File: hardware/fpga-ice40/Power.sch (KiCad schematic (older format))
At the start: 9 parts, among them J2 Conn_01x03, U8 AZ1117-1.2, U9 AZ1117-1.2

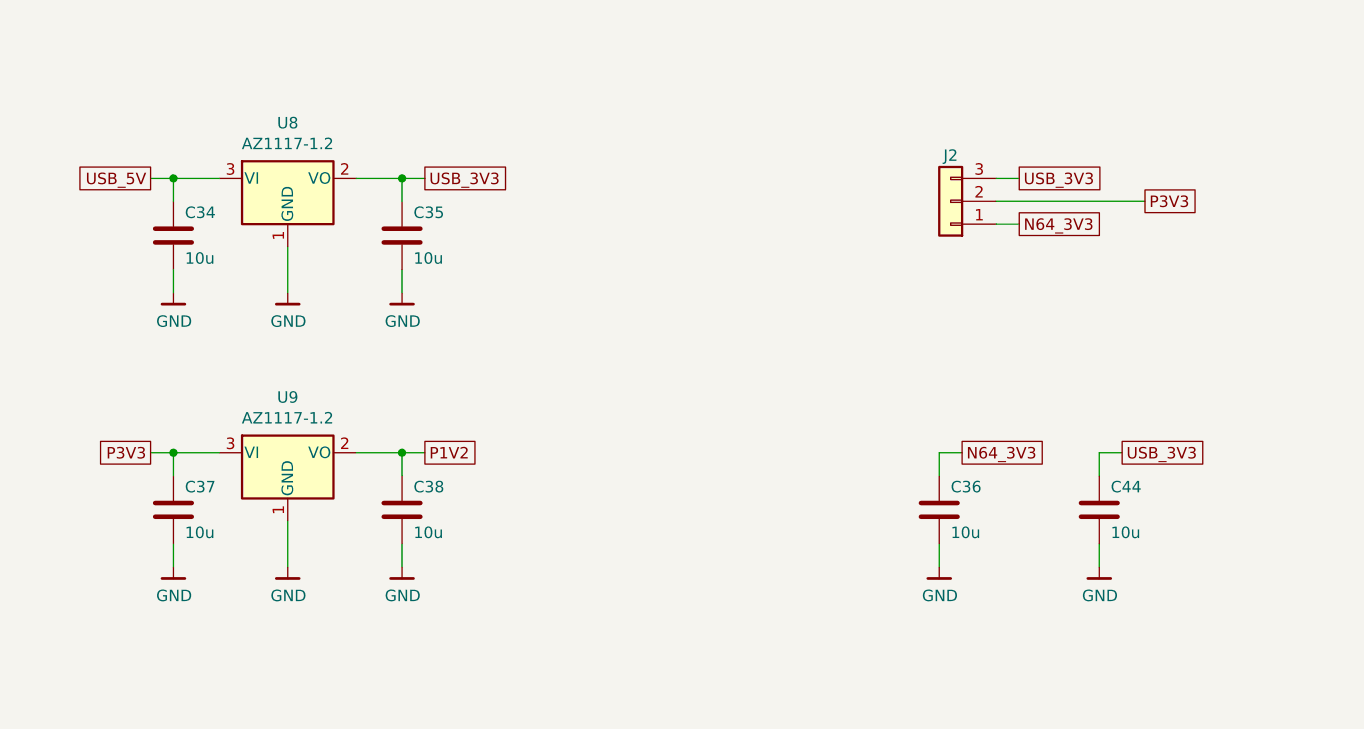
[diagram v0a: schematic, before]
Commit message: Add title and licensing info to documents
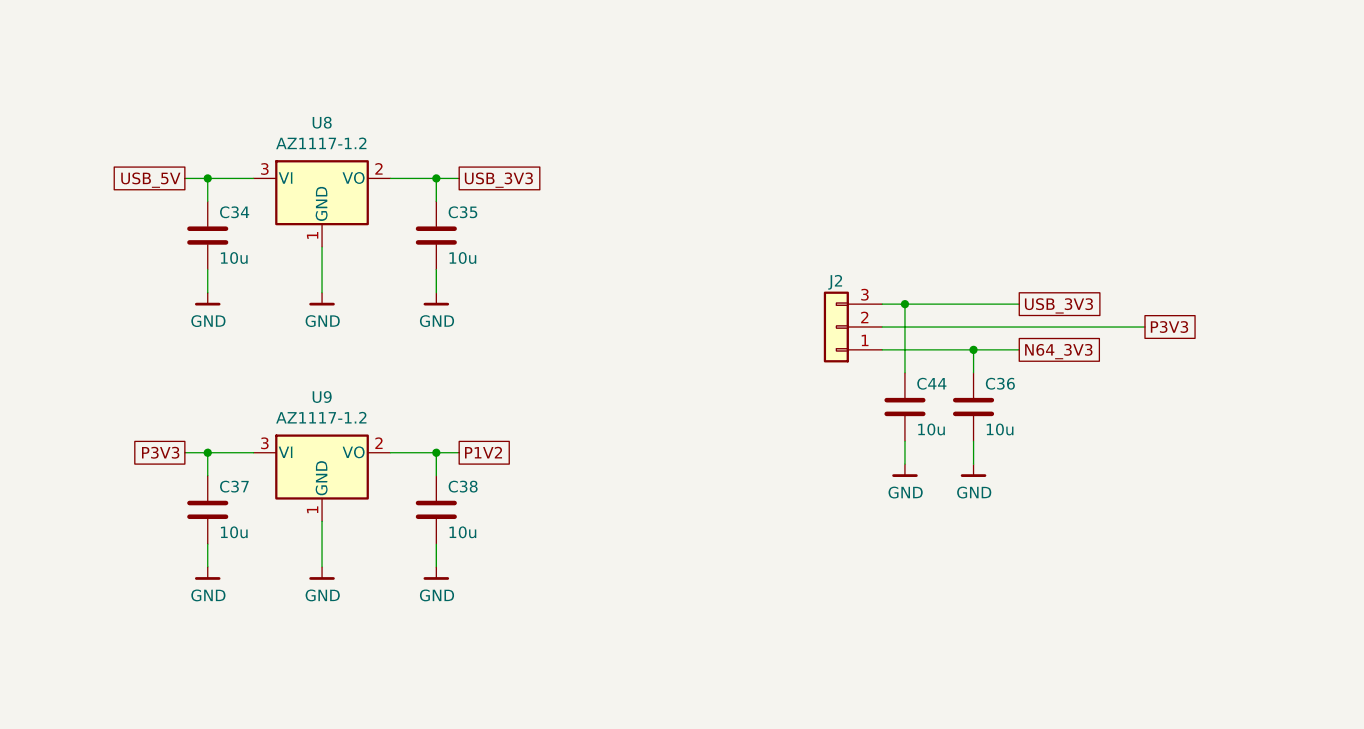
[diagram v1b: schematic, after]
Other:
- moved on the sheet: C34, C35, C36, C37, C38, C44, J2, U8, U9

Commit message: Reannotate schematic symbols
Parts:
- renumbered C34 to C1, C35 to C2, C44 to C3, C36 to C4, C37 to C5, C38 to C6, J2 to J1, U8 to U2, U9 to U3
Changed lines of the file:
@@
 P 3950 3400
 AR Path="/5F820EB8" Ref="U?"  Part="1"
-AR Path="/5F7F68FE/5F820EB8" Ref="U8"  Part="1"
-F 0 "U8" H 3950 3642 50  0000 C CNN
+AR Path="/5F7F68FE/5F820EB8" Ref="U2"  Part="1"
+F 0 "U2" H 3950 3642 50  0000 C CNN
 F 1 "AZ1117-1.2" H 3950 3551 50  0000 C CNN
 F 2 "Package_TO_SOT_SMD:SOT-223-3_TabPin2" H 3950 3650 50  0001 C CIN
@@
 P 3450 3650
 AR Path="/5F820EBE" Ref="C?"  Part="1"
-AR Path="/5F7F68FE/5F820EBE" Ref="C34"  Part="1"
-F 0 "C34" H 3500 3750 50  0000 L CNN
+AR Path="/5F7F68FE/5F820EBE" Ref="C1"  Part="1"
+F 0 "C1" H 3500 3750 50  0000 L CNN
 F 1 "10u" H 3500 3550 50  0000 L CNN
 F 2 "Capacitor_SMD:C_0805_2012Metric" H 3488 3500 50  0001 C CNN
@@
 P 4450 3650
 AR Path="/5F820EC4" Ref="C?"  Part="1"
-AR Path="/5F7F68FE/5F820EC4" Ref="C35"  Part="1"
-F 0 "C35" H 4500 3750 50  0000 L CNN
+AR Path="/5F7F68FE/5F820EC4" Ref="C2"  Part="1"
+F 0 "C2" H 4500 3750 50  0000 L CNN
 F 1 "10u" H 4500 3550 50  0000 L CNN
 F 2 "Capacitor_SMD:C_0805_2012Metric" H 4488 3500 50  0001 C CNN
@@
 P 3450 3900
 AR Path="/5F820ED2" Ref="#PWR?"  Part="1"
-AR Path="/5F7F68FE/5F820ED2" Ref="#PWR0101"  Part="1"
-F 0 "#PWR0101" H 3450 3650 50  0001 C CNN
+AR Path="/5F7F68FE/5F820ED2" Ref="#PWR01"  Part="1"
+F 0 "#PWR01" H 3450 3650 50  0001 C CNN
 F 1 "GND" H 3453 3774 50  0000 C CNN
 F 2 "" H 3350 3550 50  0001 C CNN
@@
 P 4450 3900
 AR Path="/5F820ED9" Ref="#PWR?"  Part="1"
-AR Path="/5F7F68FE/5F820ED9" Ref="#PWR0102"  Part="1"
-F 0 "#PWR0102" H 4450 3650 50  0001 C CNN
+AR Path="/5F7F68FE/5F820ED9" Ref="#PWR03"  Part="1"
+F 0 "#PWR03" H 4450 3650 50  0001 C CNN
 F 1 "GND" H 4453 3774 50  0000 C CNN
 F 2 "" H 4350 3550 50  0001 C CNN
@@
 P 3950 3900
 AR Path="/5F820EDF" Ref="#PWR?"  Part="1"
-AR Path="/5F7F68FE/5F820EDF" Ref="#PWR0103"  Part="1"
-F 0 "#PWR0103" H 3950 3650 50  0001 C CNN
+AR Path="/5F7F68FE/5F820EDF" Ref="#PWR02"  Part="1"
+F 0 "#PWR02" H 3950 3650 50  0001 C CNN
 F 1 "GND" H 3953 3774 50  0000 C CNN
 F 2 "" H 3850 3550 50  0001 C CNN
@@
 P 3950 4600
 AR Path="/5F820EE8" Ref="U?"  Part="1"
-AR Path="/5F7F68FE/5F820EE8" Ref="U9"  Part="1"
-F 0 "U9" H 3950 4842 50  0000 C CNN
+AR Path="/5F7F68FE/5F820EE8" Ref="U3"  Part="1"
+F 0 "U3" H 3950 4842 50  0000 C CNN
 F 1 "AZ1117-1.2" H 3950 4751 50  0000 C CNN
 F 2 "Package_TO_SOT_SMD:SOT-223-3_TabPin2" H 3950 4850 50  0001 C CIN
@@
 P 3450 4850
 AR Path="/5F820EEE" Ref="C?"  Part="1"
-AR Path="/5F7F68FE/5F820EEE" Ref="C37"  Part="1"
-F 0 "C37" H 3500 4950 50  0000 L CNN
+AR Path="/5F7F68FE/5F820EEE" Ref="C5"  Part="1"
+F 0 "C5" H 3500 4950 50  0000 L CNN
 F 1 "10u" H 3500 4750 50  0000 L CNN
 F 2 "Capacitor_SMD:C_0805_2012Metric" H 3488 4700 50  0001 C CNN
@@
 P 4450 4850
 AR Path="/5F820EF4" Ref="C?"  Part="1"
-AR Path="/5F7F68FE/5F820EF4" Ref="C38"  Part="1"
-F 0 "C38" H 4500 4950 50  0000 L CNN
+AR Path="/5F7F68FE/5F820EF4" Ref="C6"  Part="1"
+F 0 "C6" H 4500 4950 50  0000 L CNN
 F 1 "10u" H 4500 4750 50  0000 L CNN
 F 2 "Capacitor_SMD:C_0805_2012Metric" H 4488 4700 50  0001 C CNN
@@
 P 3450 5100
 AR Path="/5F820F02" Ref="#PWR?"  Part="1"
-AR Path="/5F7F68FE/5F820F02" Ref="#PWR0104"  Part="1"
-F 0 "#PWR0104" H 3450 4850 50  0001 C CNN
+AR Path="/5F7F68FE/5F820F02" Ref="#PWR06"  Part="1"
+F 0 "#PWR06" H 3450 4850 50  0001 C CNN
 F 1 "GND" H 3453 4974 50  0000 C CNN
 F 2 "" H 3350 4750 50  0001 C CNN
@@
 P 4450 5100
 AR Path="/5F820F09" Ref="#PWR?"  Part="1"
-AR Path="/5F7F68FE/5F820F09" Ref="#PWR0105"  Part="1"
-F 0 "#PWR0105" H 4450 4850 50  0001 C CNN
+AR Path="/5F7F68FE/5F820F09" Ref="#PWR08"  Part="1"
+F 0 "#PWR08" H 4450 4850 50  0001 C CNN
 F 1 "GND" H 4453 4974 50  0000 C CNN
 F 2 "" H 4350 4750 50  0001 C CNN
@@
 P 3950 5100
 AR Path="/5F820F0F" Ref="#PWR?"  Part="1"
-AR Path="/5F7F68FE/5F820F0F" Ref="#PWR0106"  Part="1"
-F 0 "#PWR0106" H 3950 4850 50  0001 C CNN
+AR Path="/5F7F68FE/5F820F0F" Ref="#PWR07"  Part="1"
+F 0 "#PWR07" H 3950 4850 50  0001 C CNN
 F 1 "GND" H 3953 4974 50  0000 C CNN
 F 2 "" H 3850 4750 50  0001 C CNN
@@
 P 6800 4400
 AR Path="/5F820F1C" Ref="C?"  Part="1"
-AR Path="/5F7F68FE/5F820F1C" Ref="C36"  Part="1"
-F 0 "C36" H 6850 4500 50  0000 L CNN
+AR Path="/5F7F68FE/5F820F1C" Ref="C4"  Part="1"
+F 0 "C4" H 6850 4500 50  0000 L CNN
 F 1 "10u" H 6850 4300 50  0000 L CNN
 F 2 "Capacitor_SMD:C_0805_2012Metric" H 6838 4250 50  0001 C CNN
@@
 P 6800 4650
 AR Path="/5F820F23" Ref="#PWR?"  Part="1"
-AR Path="/5F7F68FE/5F820F23" Ref="#PWR0107"  Part="1"
-F 0 "#PWR0107" H 6800 4400 50  0001 C CNN
+AR Path="/5F7F68FE/5F820F23" Ref="#PWR05"  Part="1"
+F 0 "#PWR05" H 6800 4400 50  0001 C CNN
 F 1 "GND" H 6803 4524 50  0000 C CNN
 F 2 "" H 6700 4300 50  0001 C CNN
@@
 P 6200 4050
 AR Path="/5F820F2A" Ref="J?"  Part="1"
-AR Path="/5F7F68FE/5F820F2A" Ref="J2"  Part="1"
-F 0 "J2" H 6200 3850 50  0000 C CNN
+AR Path="/5F7F68FE/5F820F2A" Ref="J1"  Part="1"
+F 0 "J1" H 6200 3850 50  0000 C CNN
 F 1 "Conn_01x03" H 6118 3816 50  0001 C CNN
 F 2 "Connector_PinHeader_2.54mm:PinHeader_1x03_P2.54mm_Vertical" H 6200 4050 50  0001 C CNN
@@
 P 6500 4400
 AR Path="/5F820F39" Ref="C?"  Part="1"
-AR Path="/5F7F68FE/5F820F39" Ref="C44"  Part="1"
-F 0 "C44" H 6550 4500 50  0000 L CNN
+AR Path="/5F7F68FE/5F820F39" Ref="C3"  Part="1"
+F 0 "C3" H 6550 4500 50  0000 L CNN
 F 1 "10u" H 6550 4300 50  0000 L CNN
 F 2 "Capacitor_SMD:C_0805_2012Metric" H 6538 4250 50  0001 C CNN
@@
 P 6500 4650
 AR Path="/5F820F40" Ref="#PWR?"  Part="1"
-AR Path="/5F7F68FE/5F820F40" Ref="#PWR0108"  Part="1"
-F 0 "#PWR0108" H 6500 4400 50  0001 C CNN
+AR Path="/5F7F68FE/5F820F40" Ref="#PWR04"  Part="1"
+F 0 "#PWR04" H 6500 4400 50  0001 C CNN
 F 1 "GND" H 6503 4524 50  0000 C CNN
 F 2 "" H 6400 4300 50  0001 C CNN

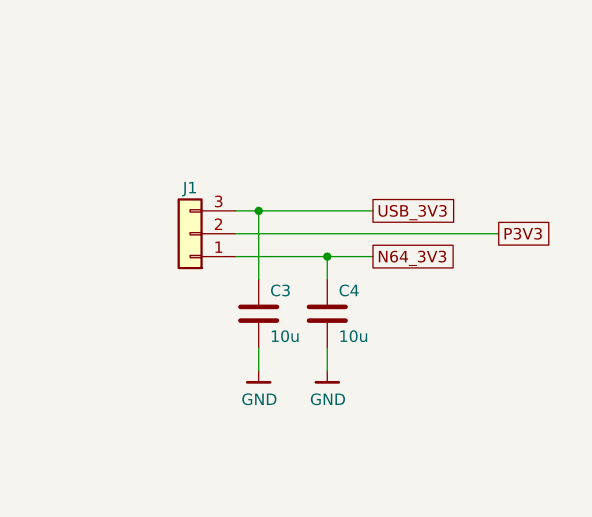
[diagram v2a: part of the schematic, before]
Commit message: Flash programming header can hold FPGA in configuration reset
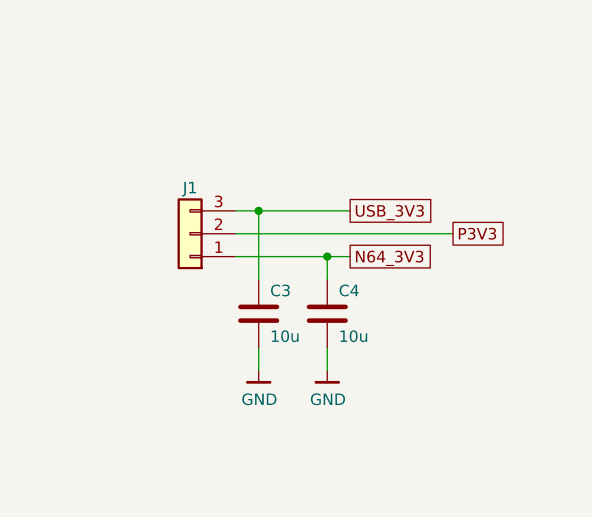
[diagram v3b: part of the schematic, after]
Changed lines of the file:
@@
 	6400 3950 6500 3950
 Wire Wire Line
-	6400 4050 7550 4050
+	6400 4050 7350 4050
 Wire Wire Line
 	6400 4150 6800 4150
-Text GLabel 7000 3950 2    50   UnSpc ~ 0
+Text GLabel 6900 3950 2    50   UnSpc ~ 0
 USB_3V3
-Text GLabel 7000 4150 2    50   UnSpc ~ 0
+Text GLabel 6900 4150 2    50   UnSpc ~ 0
 N64_3V3
-Text GLabel 7550 4050 2    50   UnSpc ~ 0
+Text GLabel 7350 4050 2    50   UnSpc ~ 0
 P3V3
 Wire Wire Line
@@
 Connection ~ 6500 3950
 Wire Wire Line
-	6500 3950 7000 3950
+	6500 3950 6900 3950
 Connection ~ 6800 4150
 Wire Wire Line
-	6800 4150 7000 4150
+	6800 4150 6900 4150
 $EndSCHEMATC

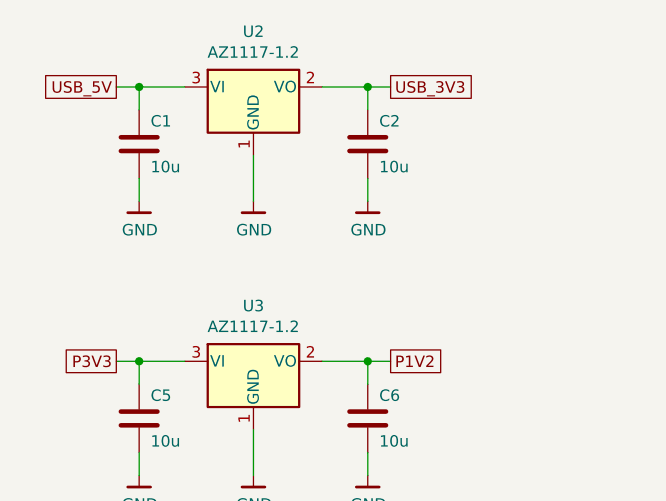
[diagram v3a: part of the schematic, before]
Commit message: Component selection by MPN and routing cleanup
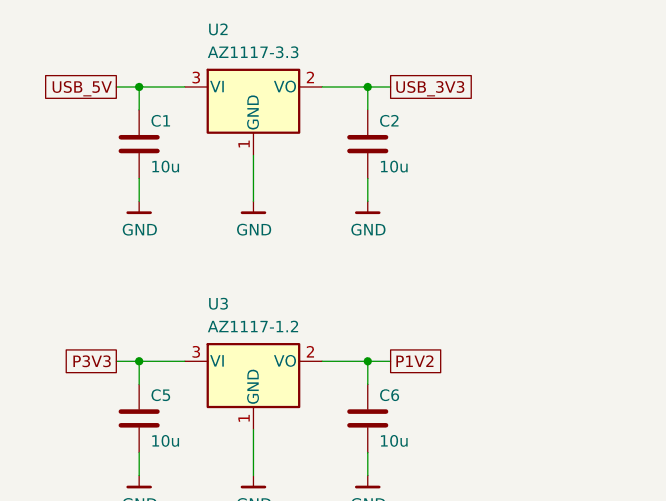
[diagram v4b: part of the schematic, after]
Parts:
- C1, C2, C3, C4, C5, C6: MPN (none) -> CL21A106KAYNNNE
- J1: MPN (none) -> C49257
- U2: value AZ1117-1.2 -> AZ1117-3.3; MPN (none) -> AZ1117H-3.3TRE1
- U3: MPN (none) -> AZ1117H-1.2TRE1
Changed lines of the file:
@@
 AR Path="/5F820EB8" Ref="U?"  Part="1"
 AR Path="/5F7F68FE/5F820EB8" Ref="U2"  Part="1"
-F 0 "U2" H 3950 3642 50  0000 C CNN
-F 1 "AZ1117-1.2" H 3950 3551 50  0000 C CNN
+F 0 "U2" H 3750 3650 50  0000 L CNN
+F 1 "AZ1117-3.3" H 3750 3550 50  0000 L CNN
 F 2 "Package_TO_SOT_SMD:SOT-223-3_TabPin2" H 3950 3650 50  0001 C CIN
 F 3 "https://www.diodes.com/assets/Datasheets/AZ1117.pdf" H 3950 3400 50  0001 C CNN
+F 4 "AZ1117H-3.3TRE1" H 3950 3400 50  0001 C CNN "MPN"
 	1    3950 3400
 	1    0    0    -1
@@
 F 2 "Capacitor_SMD:C_0805_2012Metric" H 3488 3500 50  0001 C CNN
 F 3 "~" H 3450 3650 50  0001 C CNN
+F 4 "CL21A106KAYNNNE" H 3450 3650 50  0001 C CNN "MPN"
 	1    3450 3650
 	1    0    0    -1
@@
 F 2 "Capacitor_SMD:C_0805_2012Metric" H 4488 3500 50  0001 C CNN
 F 3 "~" H 4450 3650 50  0001 C CNN
+F 4 "CL21A106KAYNNNE" H 4450 3650 50  0001 C CNN "MPN"
 	1    4450 3650
 	1    0    0    -1
@@
 AR Path="/5F820EE8" Ref="U?"  Part="1"
 AR Path="/5F7F68FE/5F820EE8" Ref="U3"  Part="1"
-F 0 "U3" H 3950 4842 50  0000 C CNN
-F 1 "AZ1117-1.2" H 3950 4751 50  0000 C CNN
+F 0 "U3" H 3750 4850 50  0000 L CNN
+F 1 "AZ1117-1.2" H 3750 4750 50  0000 L CNN
 F 2 "Package_TO_SOT_SMD:SOT-223-3_TabPin2" H 3950 4850 50  0001 C CIN
 F 3 "https://www.diodes.com/assets/Datasheets/AZ1117.pdf" H 3950 4600 50  0001 C CNN
+F 4 "AZ1117H-1.2TRE1" H 3950 4600 50  0001 C CNN "MPN"
 	1    3950 4600
 	1    0    0    -1
@@
 F 2 "Capacitor_SMD:C_0805_2012Metric" H 3488 4700 50  0001 C CNN
 F 3 "~" H 3450 4850 50  0001 C CNN
+F 4 "CL21A106KAYNNNE" H 3450 4850 50  0001 C CNN "MPN"
 	1    3450 4850
 	1    0    0    -1
@@
 F 2 "Capacitor_SMD:C_0805_2012Metric" H 4488 4700 50  0001 C CNN
 F 3 "~" H 4450 4850 50  0001 C CNN
+F 4 "CL21A106KAYNNNE" H 4450 4850 50  0001 C CNN "MPN"
 	1    4450 4850
 	1    0    0    -1
@@
 F 2 "Capacitor_SMD:C_0805_2012Metric" H 6838 4250 50  0001 C CNN
 F 3 "~" H 6800 4400 50  0001 C CNN
+F 4 "CL21A106KAYNNNE" H 6800 4400 50  0001 C CNN "MPN"
 	1    6800 4400
 	1    0    0    -1
@@
 F 2 "Connector_PinHeader_2.54mm:PinHeader_1x03_P2.54mm_Vertical" H 6200 4050 50  0001 C CNN
 F 3 "~" H 6200 4050 50  0001 C CNN
+F 4 "C49257" H 6200 4050 50  0001 C CNN "MPN"
 	1    6200 4050
 	-1   0    0    1
@@
 F 2 "Capacitor_SMD:C_0805_2012Metric" H 6538 4250 50  0001 C CNN
 F 3 "~" H 6500 4400 50  0001 C CNN
+F 4 "CL21A106KAYNNNE" H 6500 4400 50  0001 C CNN "MPN"
 	1    6500 4400
 	1    0    0    -1

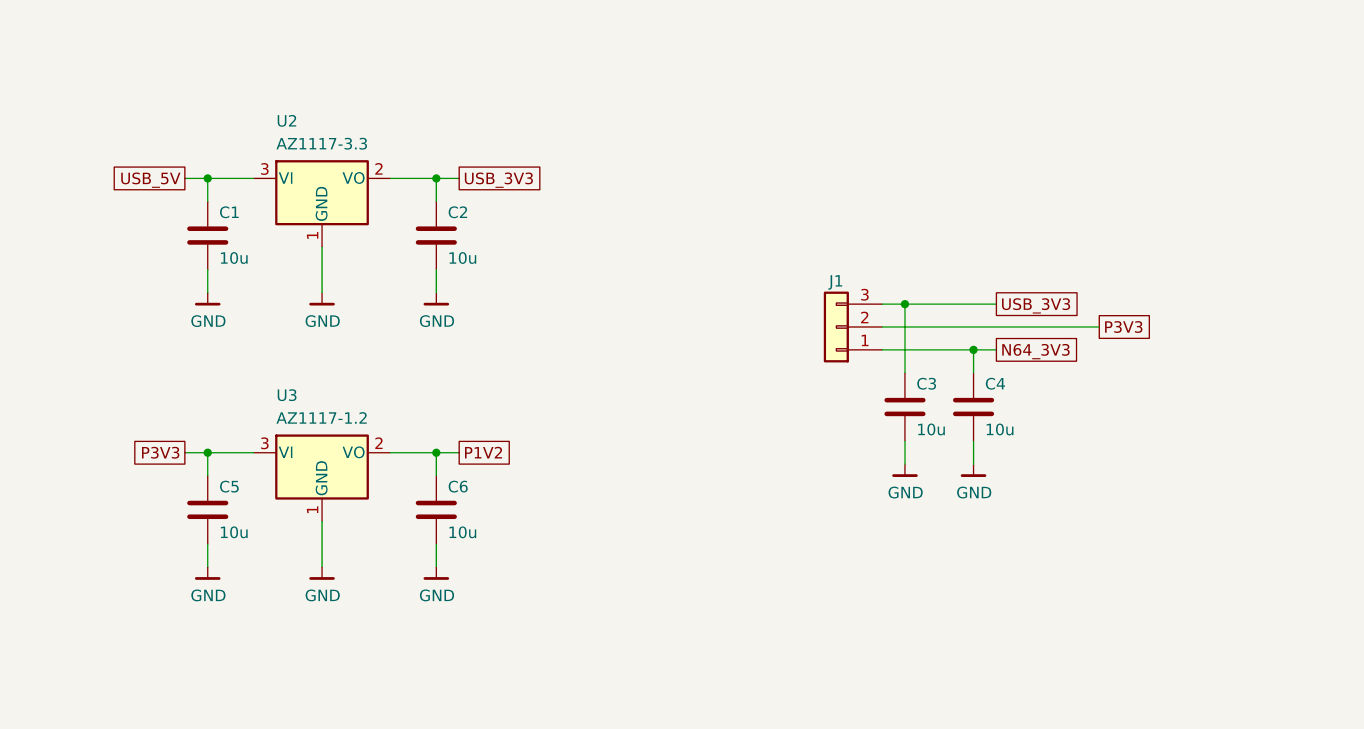
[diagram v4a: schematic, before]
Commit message: Rename SD_DET signal to SD_CD for consistency
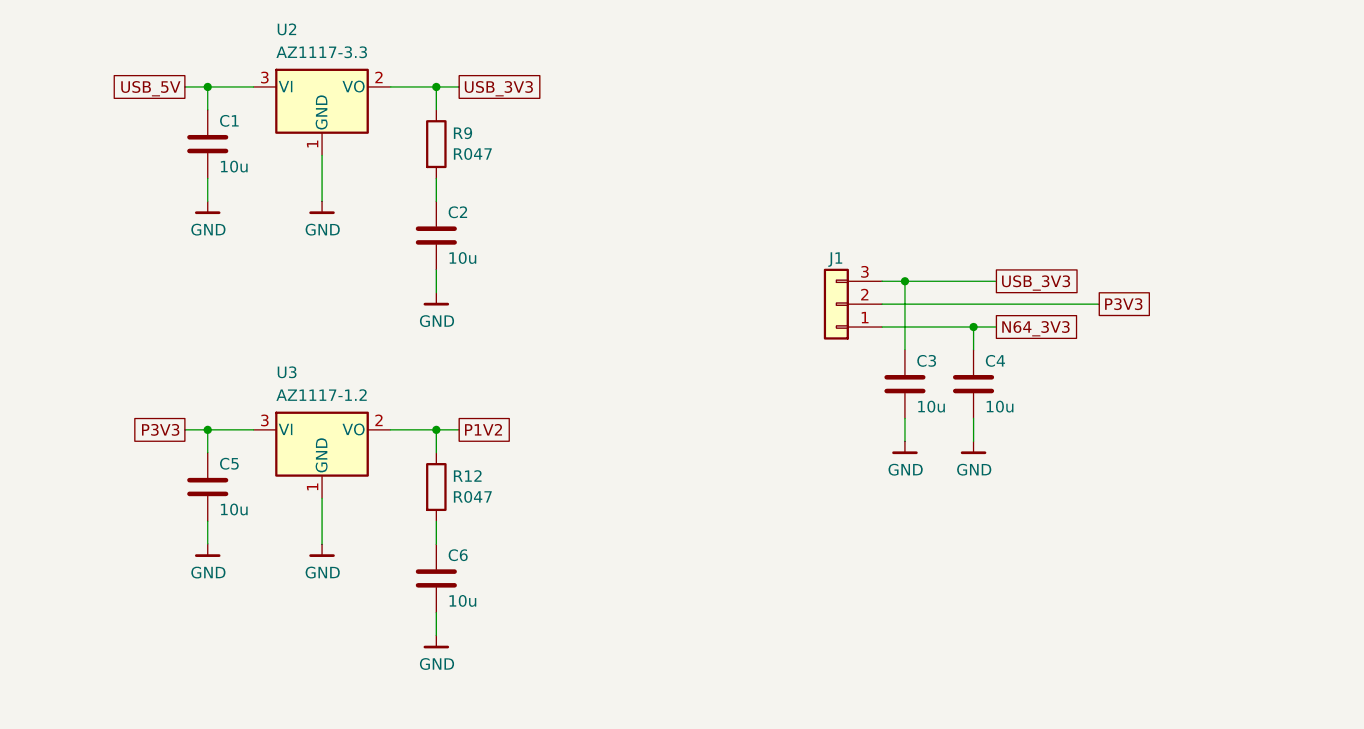
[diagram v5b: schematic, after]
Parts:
- added R12, R9: R047, Resistor_SMD:R_0603_1608Metric, symbol Device:R
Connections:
- net P1V2: now also R12.1; no longer C6.1
- net USB_3V3: now also R9.1; no longer C2.1
- new net: C2.1, R9.2
- new net: C6.1, R12.2
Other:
- moved on the sheet: C1, C3, C4, C5, C6, J1, U2, U3
